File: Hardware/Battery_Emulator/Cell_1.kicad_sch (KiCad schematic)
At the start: 0 parts

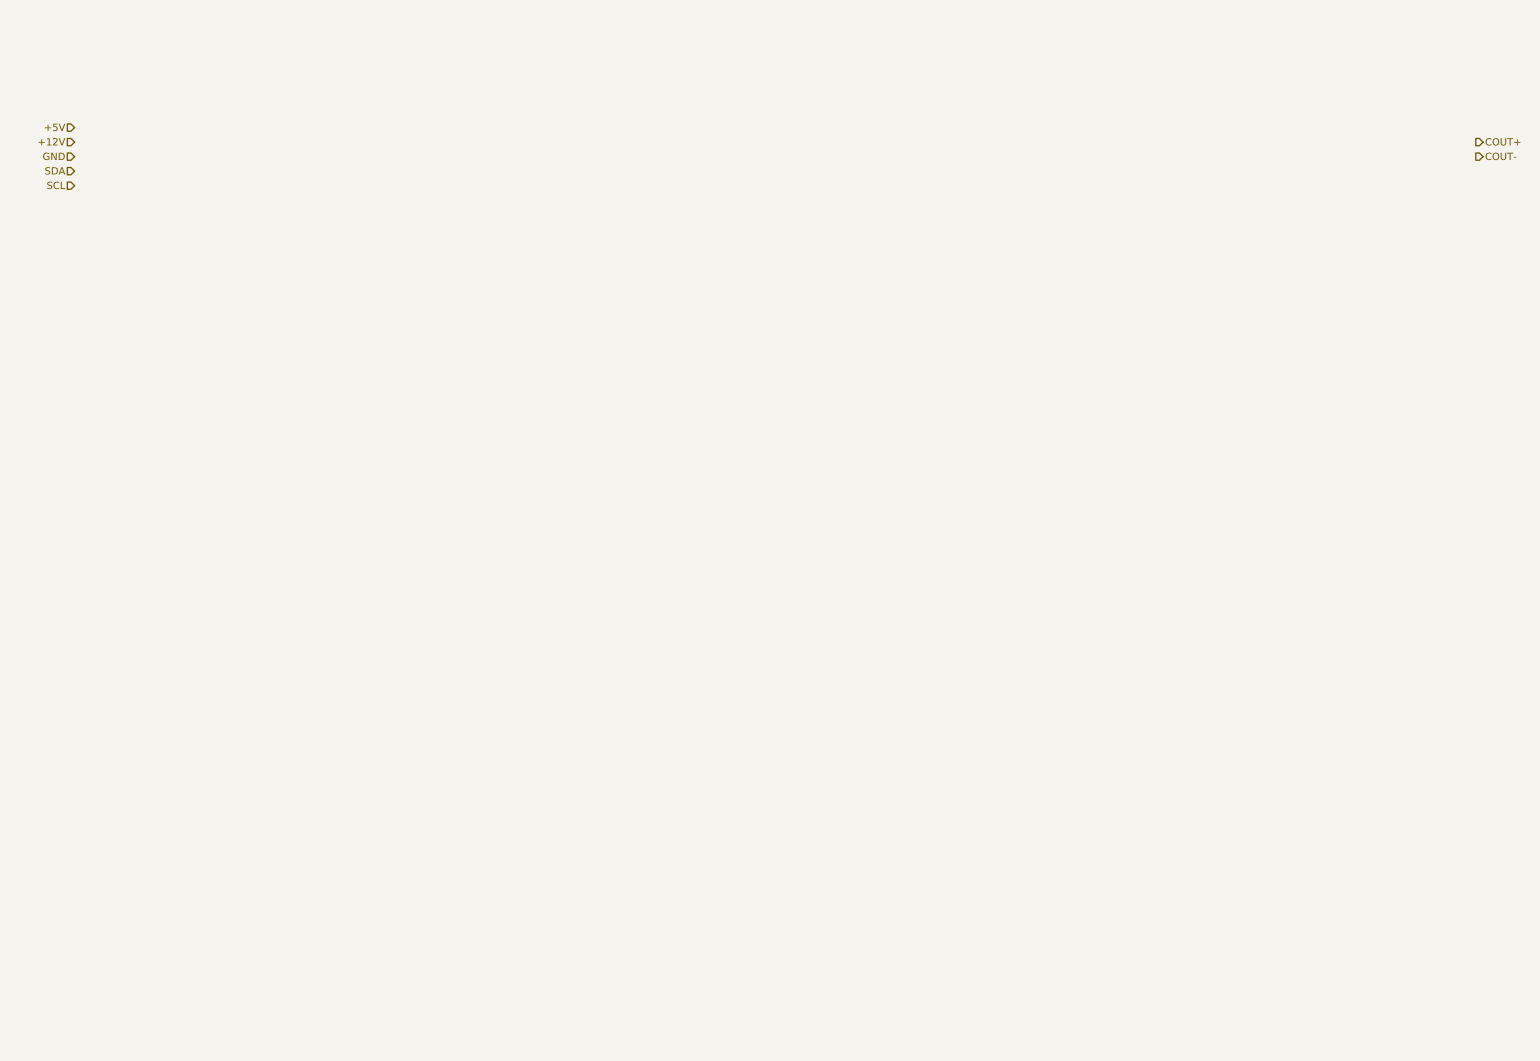
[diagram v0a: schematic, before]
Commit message: Added Cell Hierachy
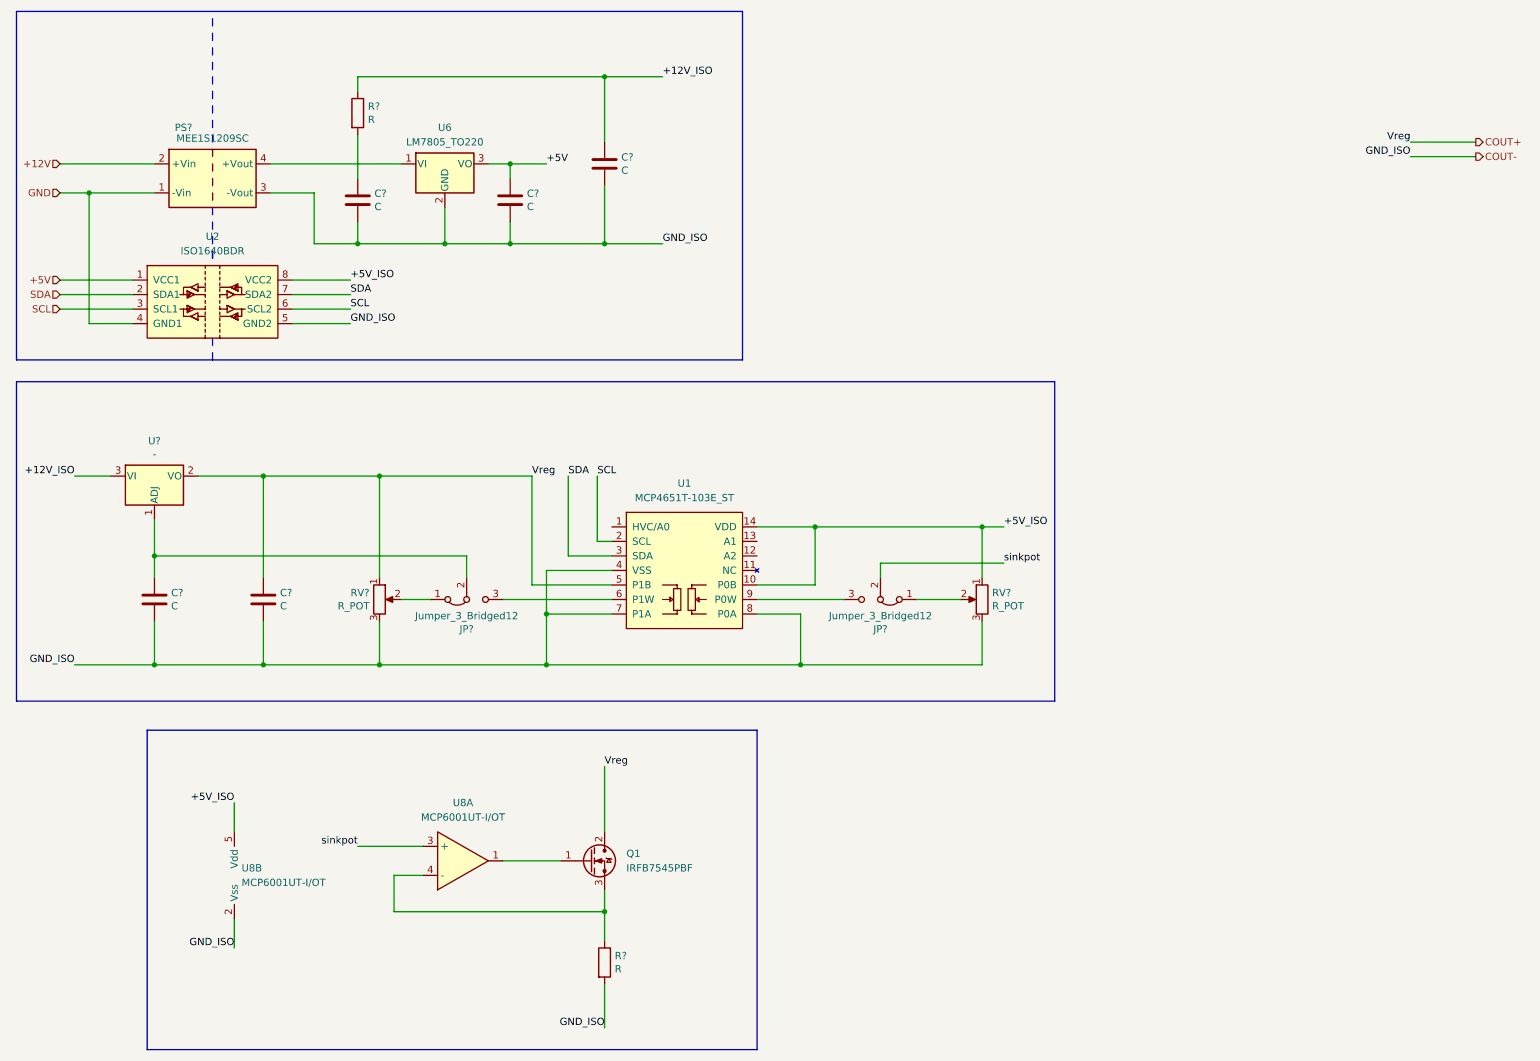
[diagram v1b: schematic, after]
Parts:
- added C? (x5): C, Capacitor_SMD:C_0805_2012Metric, symbol Device:C
- added JP? (x2): Jumper_3_Bridged12, symbol Jumper:Jumper_3_Bridged12
- added PS?: MEE1S1209SC, Converter_DCDC:Converter_DCDC_Murata_MEE1SxxxxSC_THT, symbol Converter_DCDC:MEE1S1209SC
- added Q1: IRFB7545PBF, Package_TO_SOT_THT:TO-220-3_Horizontal_TabUp, symbol PR7 Custom:IRFB7545PBF
- added R? (x2): R, Resistor_SMD:R_0805_2012Metric, symbol Device:R
- added RV? (x2): R_POT, symbol Device:R_POT
- added U1: MCP4651T-103E_ST, Package_SO:TSSOP-14_4.4x5mm_P0.65mm, symbol PR7 Custom:MCP4651T-103E_ST
- added U2: ISO1640BDR, Package_SO:SO-8_3.9x4.9mm_P1.27mm, symbol PR7 Custom:ISO1640BDR
- added U6: LM7805_TO220, Package_TO_SOT_THT:TO-220-3_Vertical, symbol Regulator_Linear:LM7805_TO220
- added U8: MCP6001UT-I/OT, Package_TO_SOT_SMD:SOT-23-5, symbol PR7 Custom:MCP6001UT-I/OT
- added U?: -, Package_SO:TSSOP-8_3x3mm_P0.65mm, symbol Regulator_Linear:LM317L_TO92
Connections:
- net +12V: now also PS?.2 (+Vin)
- net +5V: now also C?.1, U2.1 (VCC1), U6.3 (VO)
- net COUT+: now also C?.1, Q1.2, Q1.7 (D), RV?.1, U1.5 (P1B), U?.2 (VO)
- net COUT-: now also C?.2, C?.2, C?.2, C?.2, C?.2, PS?.3 (-Vout), R?.2, RV?.3, RV?.3, U1.4 (VSS), U1.7 (P1A), U1.8 (P0A), U2.5 (GND2), U6.2 (GND), U8.2 (Vss)
- net GND: now also PS?.1 (-Vin), U2.4 (GND1)
- net SCL: now also U1.2 (SCL), U2.3 (SCL1), U2.6 (SCL2)
- net SDA: now also U1.3 (SDA), U2.2 (SDA1), U2.7 (SDA2)
- new net: JP?.1 (A), RV?.2 (x2)
- new net: JP?.3 (B), U1.9 (P0W)
- new net: C?.1, JP?.2 (C), U?.1 (ADJ)
- new net: JP?.3 (B), U1.6 (P1W)
- new net: C?.1, R?.2
- new net: Q1.1, U8.1
- new net: Q1.3, R?.1, U8.4 (-)
- new net: PS?.4 (+Vout), U6.1 (VI)
- new net +12V_ISO: C?.1, R?.1, U?.3 (VI)
- new net +5V_ISO: RV?.1, U1.10 (P0B), U1.14 (VDD), U2.8 (VCC2), U8.5 (Vdd)
- new net sinkpot: JP?.2 (C), U8.3 (+)

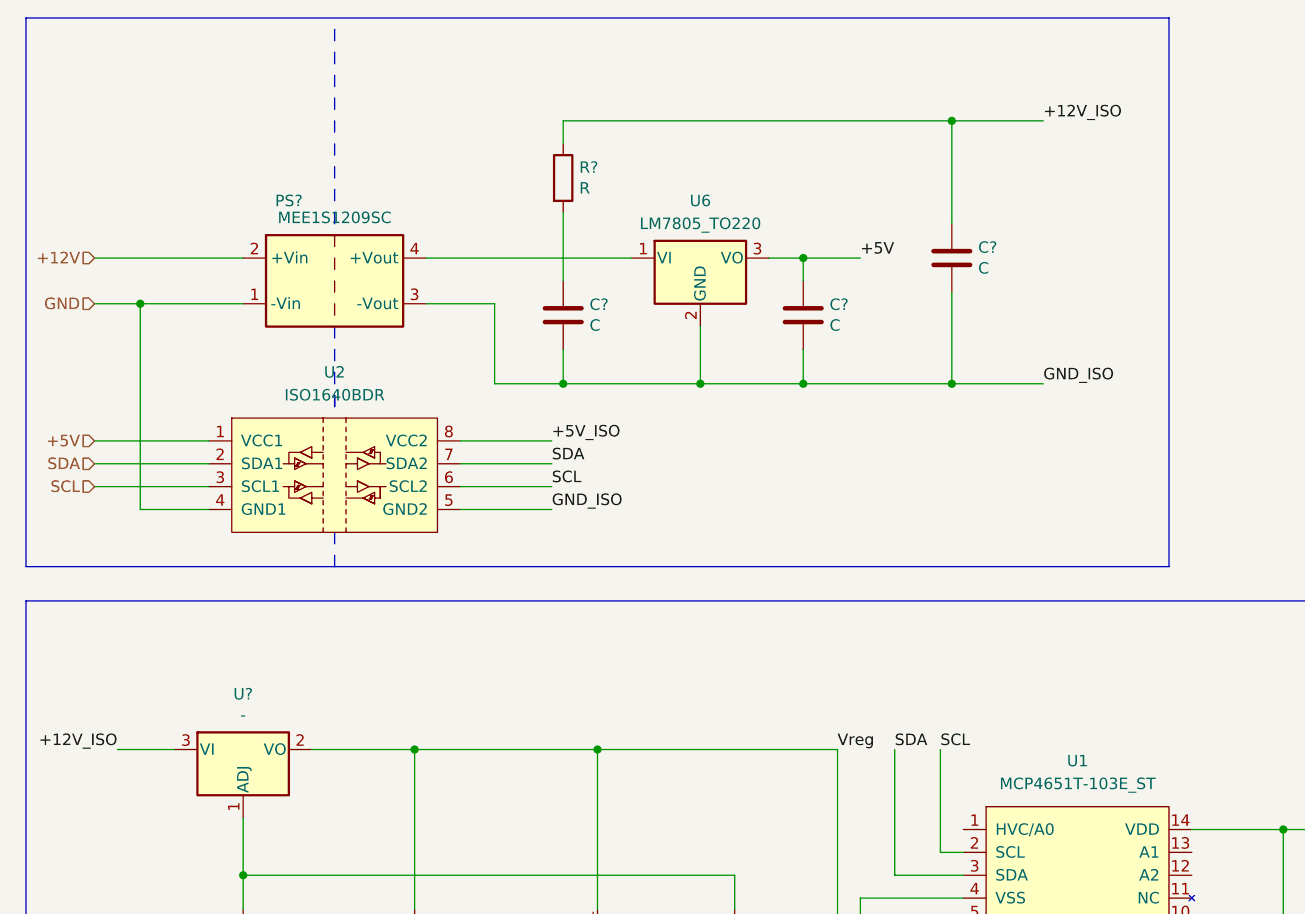
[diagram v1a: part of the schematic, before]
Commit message: Added ATMega and fixed isolated voltage level
12V_ISO -> 9V_ISO
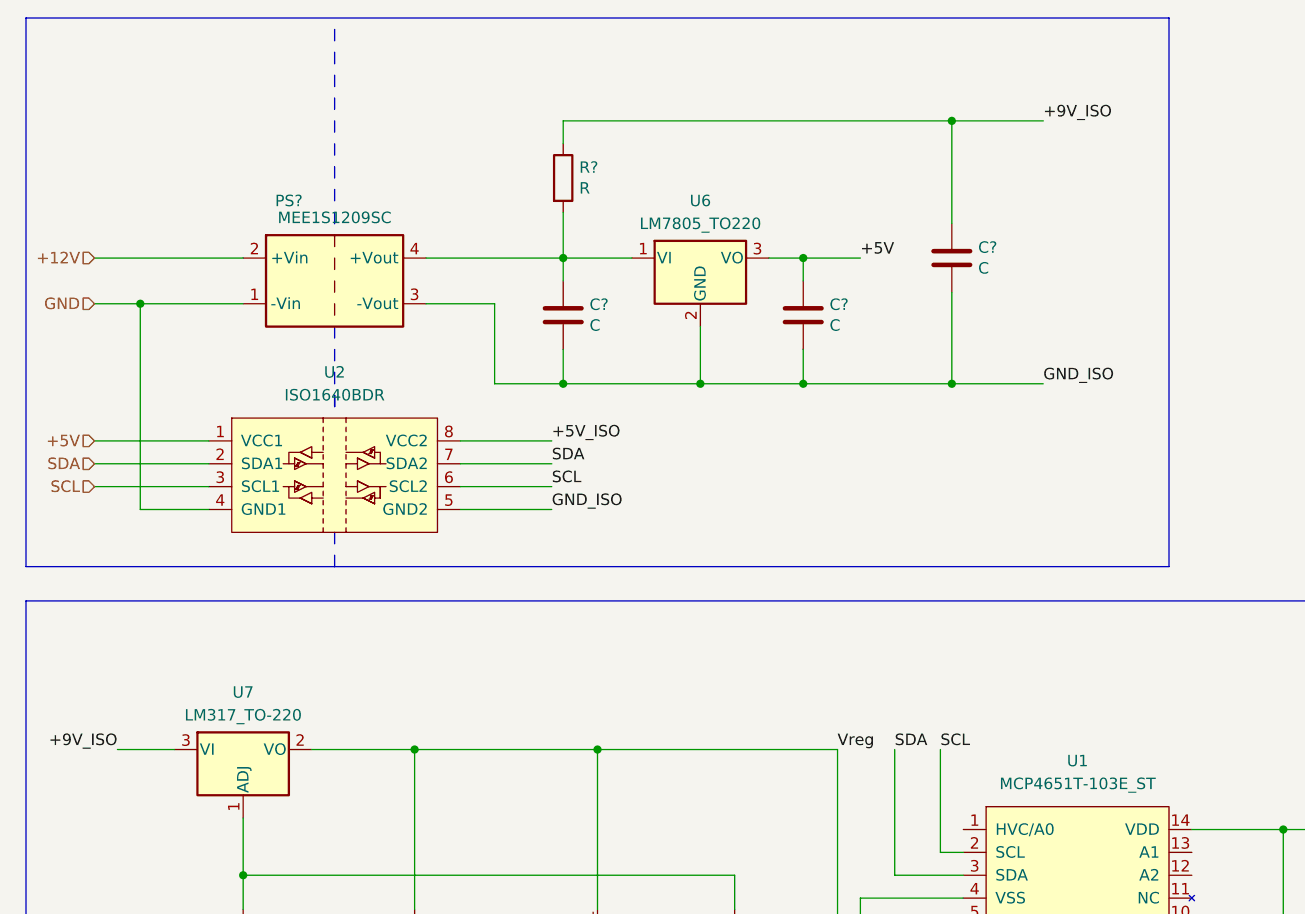
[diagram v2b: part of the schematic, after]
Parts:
- removed U?: -, Package_SO:TSSOP-8_3x3mm_P0.65mm, symbol Regulator_Linear:LM317L_TO92
- added U7: LM317_TO-220, Package_TO_SOT_THT:TO-220-3_Horizontal_TabUp, symbol Regulator_Linear:LM317_TO-220
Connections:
- net COUT+: now also U7.2 (VO)
- net at C?.1, JP?.2 (C): now also U7.1 (ADJ)
- net at C?.1, R?.2: now also PS?.4 (+Vout), U6.1 (VI)
- net +12V_ISO renamed +9V_ISO
- net +9V_ISO: now also U7.3 (VI)
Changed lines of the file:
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@@
   (junction (at 92.71 53.34) (diameter 0) (color 0 0 0 0)
   )
+  (junction (at 77.47 39.37) (diameter 0) (color 0 0 0 0)
+  )
   (junction (at 186.69 102.87) (diameter 0) (color 0 0 0 0)
   )
@@
     (stroke (width 0) (type default))
   )
+  (wire (pts (xy 77.47 39.37) (xy 85.09 39.37))
+    (stroke (width 0) (type default))
+  )
   (polyline (pts (xy 52.07 31.75) (xy 52.07 33.02))
     (stroke (width 0) (type default))
@@
     (stroke (width 0) (type default))
   )
+  (wire (pts (xy 77.47 34.29) (xy 77.47 39.37))
+    (stroke (width 0) (type default))
+  )
   (polyline (pts (xy 52.07 24.13) (xy 52.07 25.4))
     (stroke (width 0) (type default))
@@
     (stroke (width 0) (type default))
   )
+  (wire (pts (xy 77.47 39.37) (xy 77.47 41.91))
+    (stroke (width 0) (type default))
+  )
   (wire (pts (xy 121.92 107.95) (xy 114.3 107.95))
     (stroke (width 0) (type default))
@@
     (stroke (width 0) (type default))
   )
-  (wire (pts (xy 77.47 34.29) (xy 77.47 41.91))
-    (stroke (width 0) (type default))
-  )
   (wire (pts (xy 186.69 127) (xy 154.94 127))
     (stroke (width 0) (type default))
@@
     (stroke (width 0) (type default))
   )
-  (wire (pts (xy 62.23 39.37) (xy 85.09 39.37))
+  (wire (pts (xy 62.23 39.37) (xy 77.47 39.37))
     (stroke (width 0) (type default))
   )
@@
     (effects (font (size 1.27 1.27)) (justify left bottom))
   )
-  (label "+12V_ISO" (at 130.81 24.13 0) (fields_autoplaced)
+  (label "+9V_ISO" (at 130.81 24.13 0) (fields_autoplaced)
     (effects (font (size 1.27 1.27)) (justify left bottom))
   )
@@
     (effects (font (size 1.27 1.27)) (justify left bottom))
   )
-  (label "+12V_ISO" (at 27.94 93.98 180) (fields_autoplaced)
+  (label "+9V_ISO" (at 27.94 93.98 180) (fields_autoplaced)
     (effects (font (size 1.27 1.27)) (justify right bottom))
   )
@@
     )
   )
-  (symbol (lib_id "Regulator_Linear:LM317L_TO92") (at 41.91 93.98 0) (unit 1)
-    (in_bom yes) (on_board yes) (dnp no)
-    (property "Reference" "U?" (at 41.91 87.8332 0)
-      (effects (font (size 1.27 1.27)))
-    )
-    (property "Value" "-" (at 41.91 90.1446 0)
-      (effects (font (size 1.27 1.27)))
-    )
-    (property "Footprint" "Package_SO:TSSOP-8_3x3mm_P0.65mm" (at 41.91 88.265 0)
-      (effects (font (size 1.27 1.27) italic) hide)
-    )
-    (property "Datasheet" "-" (at 41.91 93.98 0)
-      (effects (font (size 1.27 1.27)) hide)
-    )
-    (pin "1")
-    (pin "2")
-    (pin "3")
-    (instances
-      (project "Battery_Emulator"
-        (path "/bb7641ff-0dfd-4f4a-b3be-57afbbb9fdac"
-          (reference "U?") (unit 1)
-        )
-        (path "/bb7641ff-0dfd-4f4a-b3be-57afbbb9fdac/86a0f187-fc20-4f8c-b621-2752c8234446"
-          (reference "U7") (unit 1)
-        )
-      )
-    )
-  )
   (symbol (lib_id "Jumper:Jumper_3_Bridged12") (at 96.52 115.57 0) (mirror x) (unit 1)
     (in_bom yes) (on_board yes) (dnp no)
@@
         )
       )
+    )
+  )
+  (symbol (lib_id "Regulator_Linear:LM317_TO-220") (at 41.91 93.98 0) (unit 1)
+    (in_bom yes) (on_board yes) (dnp no) (fields_autoplaced)
+    (property "Reference" "U7" (at 41.91 87.63 0)
+      (effects (font (size 1.27 1.27)))
+    )
+    (property "Value" "LM317_TO-220" (at 41.91 90.17 0)
+      (effects (font (size 1.27 1.27)))
+    )
+    (property "Footprint" "Package_TO_SOT_THT:TO-220-3_Horizontal_TabUp" (at 41.91 87.63 0)
+      (effects (font (size 1.27 1.27) italic) hide)
+    )
+    (property "Datasheet" "http://www.ti.com/lit/ds/symlink/lm317.pdf" (at 41.91 93.98 0)
+      (effects (font (size 1.27 1.27)) hide)
+    )
+    (pin "1")
+    (pin "2")
+    (pin "3")
+    (instances
+      (project "Battery_Emulator"
+        (path "/bb7641ff-0dfd-4f4a-b3be-57afbbb9fdac/86a0f187-fc20-4f8c-b621-2752c8234446"
+          (reference "U7") (unit 1)
+        )
+      )
